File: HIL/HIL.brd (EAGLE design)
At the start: 129.6 x 103.7 mm, 249 parts, among them J1 JTAG_ARM_10PIN, J4 JTAG_ARM_10PIN, U1 CD74HC4067SM96, U10 INA219AIDCNR, U11 INA219AIDCNR, U12 INA219AIDCNR, U13 TM4C1294NCPDT, U14 ADUM1201ARZ, U15 SN65HVD230D, U16 TL1963AKTTR., U17 FT230XS, U2 TL1963AKTTR., U3 CD74HC4067SM96, U4 CD74HC4067SM96, U5 MCP4725A0T-E/CH, U6 TL1963AKTTR., U7 MCP2003-E/SN, U9 INA219AIDCNR, X1 A1944-50, X2 A1944-50, X4 A1944-50, Y3 NX3225GA

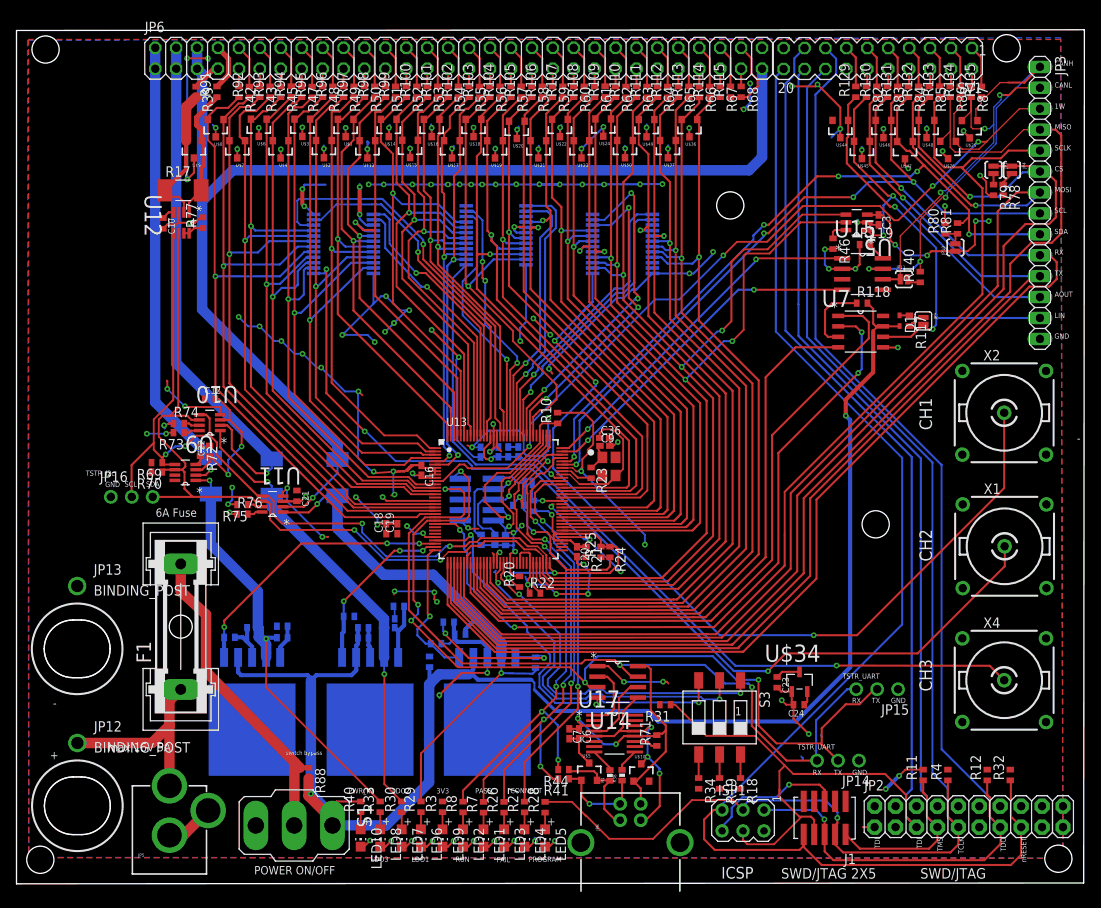
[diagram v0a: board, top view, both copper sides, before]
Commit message: Generate pdfs, and gerbers Libraries “>NAME” parameter change
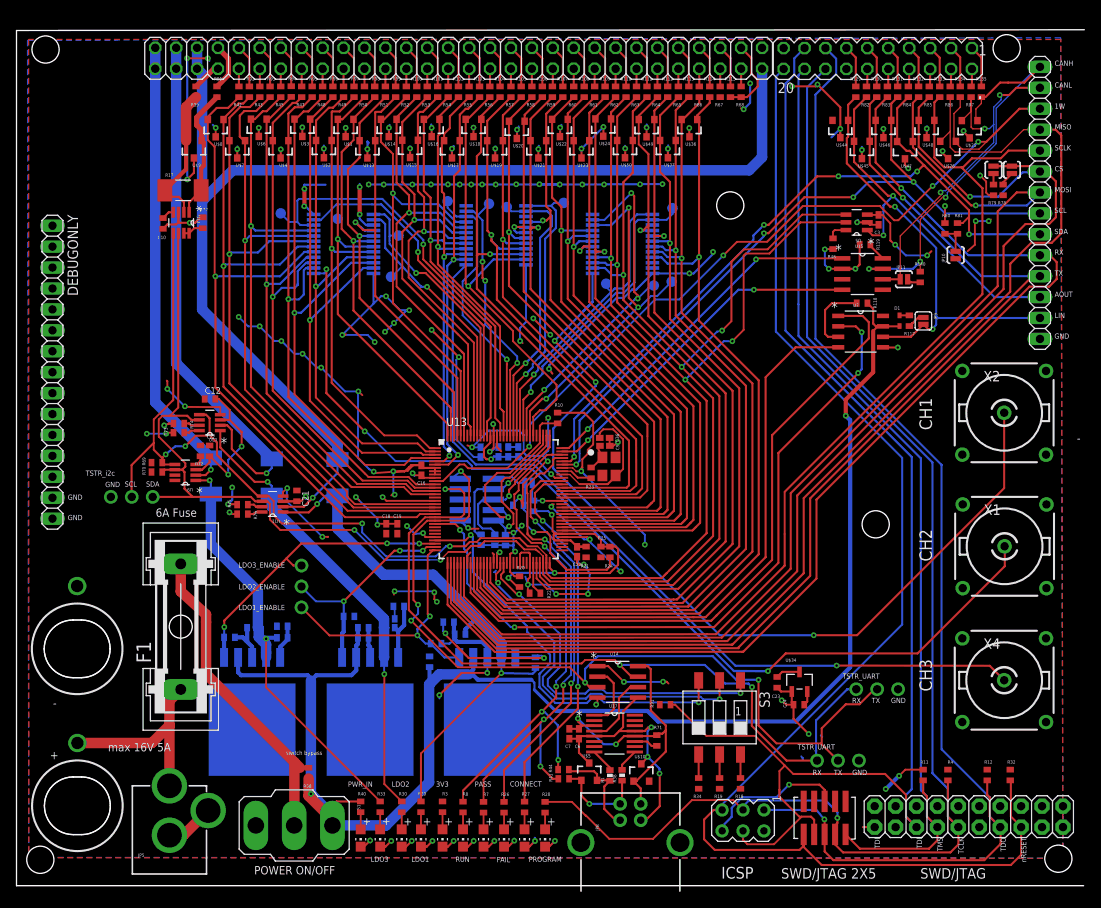
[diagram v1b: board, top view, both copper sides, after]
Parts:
- added DEBUGONLY: (no value), JDT-1800_smahed:1X15
- added JP18: (no value), JDT-1800_smahed:1X03-CLEANBIG
- added M0S0, M0S1, M0S2, M0S3: TPB1,27, testpad:B1,27
- added M1S0, M1S1, M1S2, M1S3, M2S0, M2S1, M2S2, M2S3: M0S3, testpad:B1,27
- STANDOFF1, STANDOFF5: device SparkFun-Electromechanical:STAND-OFF -> SparkFun-Electromechanical:STAND-OFF@1
- moved JP10 0.91 mm to (114.0, 76.6)
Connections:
- net GND: now also DEBUGONLY.14, DEBUGONLY.15
- net LDO1_ENABLE: now also JP18.1
- net LDO2_ENABLE: now also JP18.2
- net LDO3_ENABLE: now also JP18.3
- net M0S0: now also M0S0.TP
- net M0S1: now also M0S1.TP
- net M0S2: now also M0S2.TP
- net M0S3: now also M0S3.TP
- net M1S0: now also M1S0.TP
- net M1S1: now also M1S1.TP
- net M1S2: now also M1S2.TP
- net M1S3: now also M1S3.TP
- net M2S0: now also M2S0.TP
- net M2S1: now also M2S1.TP
- net M2S2: now also M2S2.TP
- net M2S3: now also M2S3.TP
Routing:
- net LDO1_ENABLE: track 17.8 -> 33.3 mm, vias 1 -> 2
- net LDO2_ENABLE: track 20.7 -> 26.6 mm
- net M2S0: track 39.1 -> 44.5 mm
- net TSTR_3V3: track 321.6 -> 317.2 mm
- net M0S3: track 30.6 -> 34.1 mm
- net M2S2: track 34.3 -> 37.7 mm
- net M2S1: track 41.6 -> 44.2 mm
- net M0S1: track 32.0 -> 34.5 mm
- net M1S0: track 49.5 -> 51.9 mm
- net LDO3_ENABLE: track 33.9 -> 36.1 mm
- net M0S2: track 30.7 -> 32.7 mm
- net M1S2: track 32.2 -> 34.1 mm
- net M1S1: track 43.1 -> 44.9 mm
- net M0S0: track 34.5 -> 36.1 mm
- net M2S3: track 35.2 -> 36.4 mm
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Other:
- board size 129.6 x 103.7 mm -> 129.6 x 103.9 mm
- board text added: "LDO1_ENABLE"
- board text added: "LDO2_ENABLE"
- board text added: "LDO3_ENABLE"

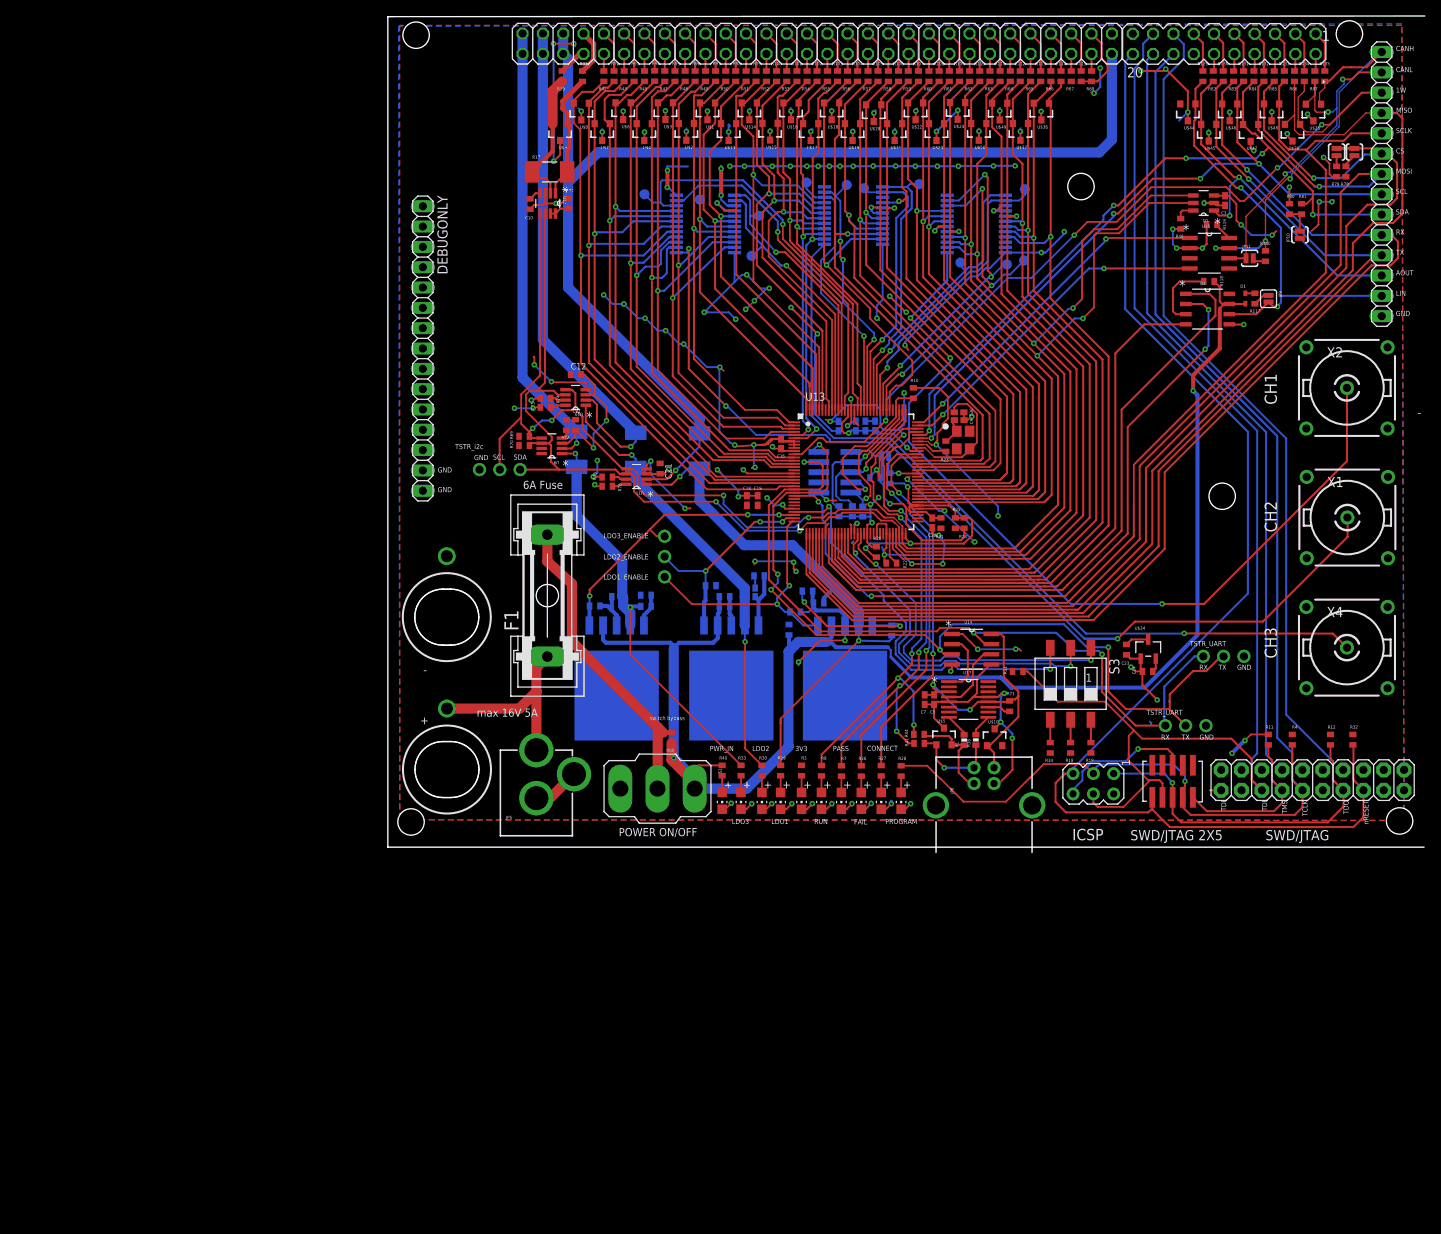
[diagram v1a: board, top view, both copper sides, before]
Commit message: Fix:   - Vcc pin present in the schematic Add: - digital tersistor to the schematic          - measurements of the holes/drills
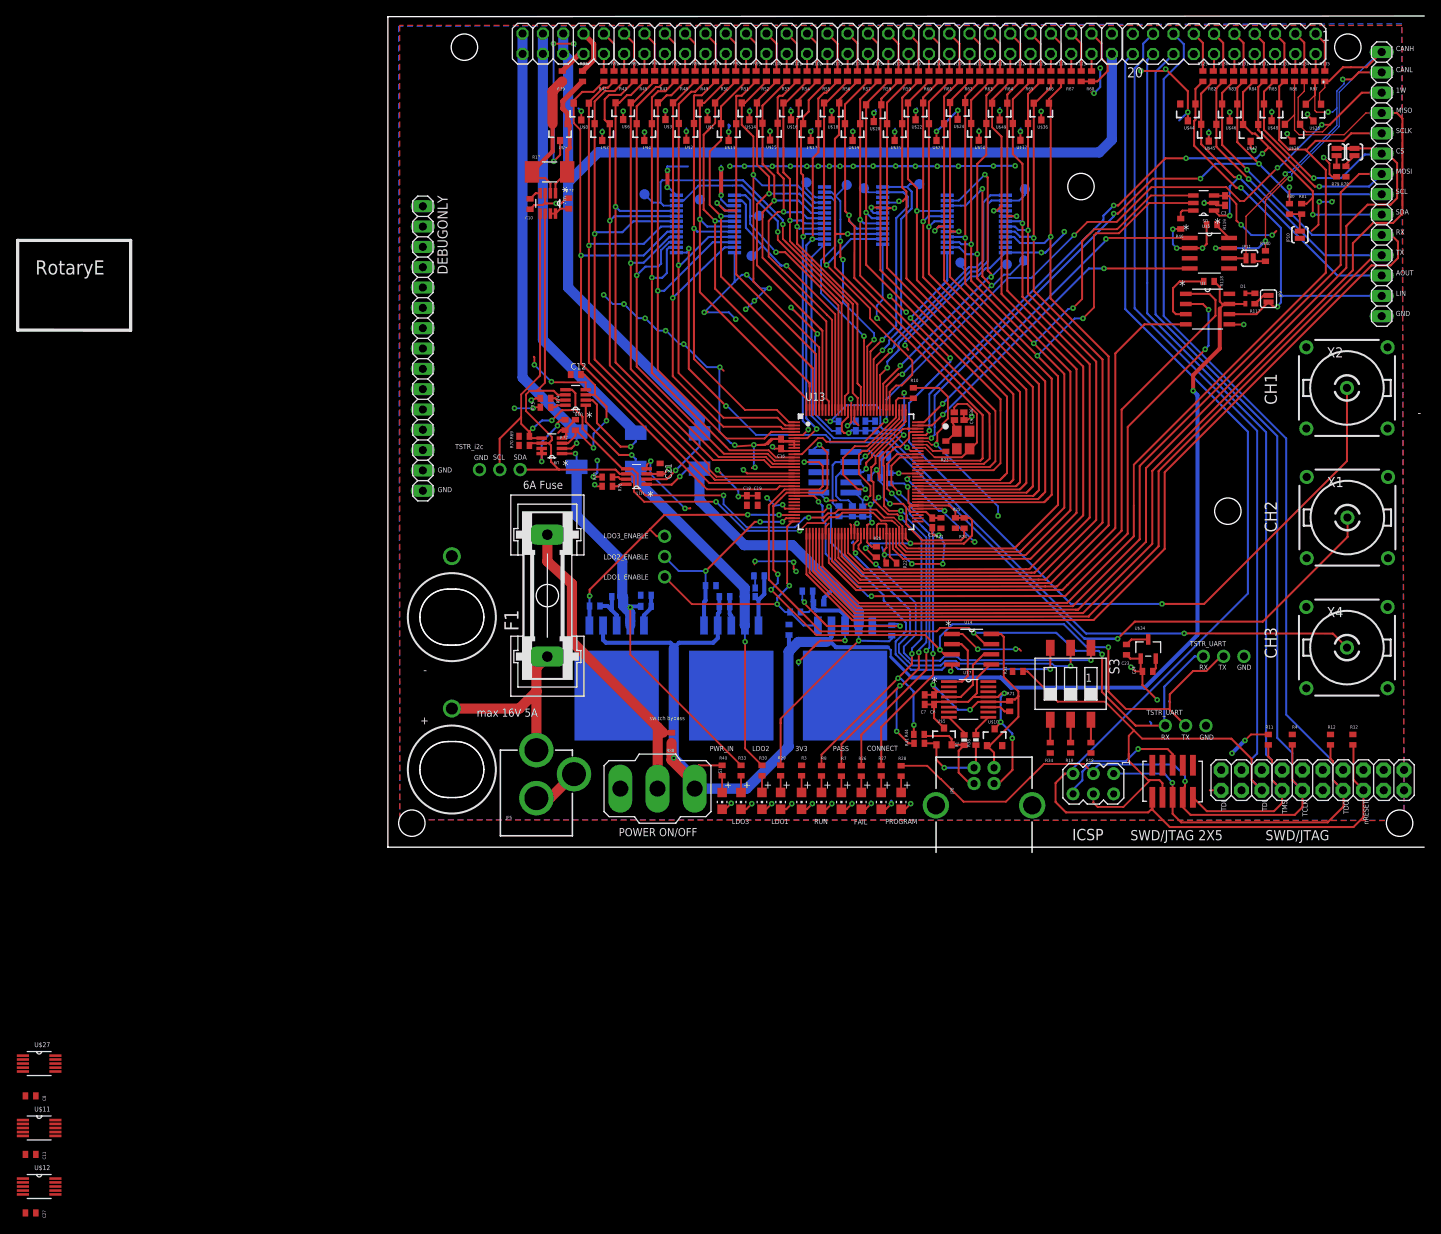
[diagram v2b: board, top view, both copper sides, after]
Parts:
- added C11, C27, C8: 0.1uF, rcl:C0402
- added U$11, U$12, U$27: DS3501, Digital resistor:DS3501
- moved STANDOFF3 6.22 mm to (9.57, 100.0)
- moved STANDOFF4 2.00 mm to (105.0, 42.0)
- moved STANDOFF2 1.66 mm to (120.0, 100.0)
- moved JP13 0.63 mm to (8.00, 28.8)
- moved JP12 0.61 mm to (8.00, 9.70)
- moved STANDOFF6 0.28 mm to (126.5, 3.00)
- moved STANDOFF1 0.18 mm to (3.00, 3.00)
- moved R72 0.18 mm to (22.1, 52.8)
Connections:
- removed net VCC: R72.2, U9.4
- new net AS: R72.1, U9.7, U9.8
- new net N$53: U$11.A1
- new net N$54: U$11.A0
- new net N$55: U$11.RH
- new net N$56: U$11.RW
- new net N$57: U$11.RL, U$11.V+
- new net N$63: U$12.A1
- new net N$66: U$12.A0
- new net N$67: U$12.RH
- new net N$68: U$12.RW
- new net N$69: U$12.RL, U$12.V+
- new net N$70: U$27.A1
- new net N$71: U$27.A0
- new net N$72: U$27.RH
- new net N$73: U$27.RW
- new net N$74: U$27.RL, U$27.V+
- net GND: now also C11.2, C27.2, C8.2, U$11.GND, U$12.GND, U$27.GND
- net TSTR_3V3: now also C11.1, C27.1, C8.1, R72.2, U$11.VCC, U$12.VCC, U$27.VCC, U9.4; no longer R72.1, U9.7, U9.8
- net TSTR_SCL: now also U$11.SCL, U$12.SCL, U$27.SCL
- net TSTR_SDA: now also U$11.SDA, U$12.SDA, U$27.SDA
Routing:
- net AS: track 0.00 -> 9.30 mm, vias 0 -> 2
- net TSTR_3V3: track 317.2 -> 321.4 mm
- net VCC: track 1.31 -> 0.00 mm
- net N$40: track 24.3 -> 23.7 mm
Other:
- board size 129.6 x 103.9 mm -> 129.5 x 103.9 mm
- board text added: "RotaryE"
